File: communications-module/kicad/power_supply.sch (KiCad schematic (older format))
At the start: 25 parts, among them J1 IDC12, P2 USB_A, P3 USB_A, P4 USB_A, P5 BACKUP, U3 TPS2064, U4 PWR_CONN, U5 TPS2064

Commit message: Communications Module update
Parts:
- JP11, JP12, JP3, JP4: footprint (none) -> Socket_Strips:Socket_Strip_Straight_1x02_Pitch2.54mm
- P2, P3, P4: footprint (none) -> USB_A_receptacle:USB_A_receptacle
- R3: footprint (none) -> 0603_handsolder:0603_HandSoldering
- U4: footprint (none) -> Socket_Strips:Socket_Strip_Straight_2x05_Pitch2.54mm
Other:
- note added: "footprint ?"
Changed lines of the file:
@@
 F 0 "P3" H 6285 5150 50  0000 C CNN
 F 1 "USB_A" H 6025 5330 50  0000 C CNN
-F 2 "" V 6025 5030 60  0000 C CNN
+F 2 "USB_A_receptacle:USB_A_receptacle" V 6025 5030 60  0001 C CNN
 F 3 "" V 6025 5030 60  0000 C CNN
 	1    6075 5130
@@
 F 0 "P4" H 8270 5150 50  0000 C CNN
 F 1 "USB_A" H 8010 5330 50  0000 C CNN
-F 2 "" V 8010 5030 60  0000 C CNN
+F 2 "USB_A_receptacle:USB_A_receptacle" V 8010 5030 60  0001 C CNN
 F 3 "" V 8010 5030 60  0000 C CNN
 	1    8060 5130
@@
 F 0 "P2" H 4295 5150 50  0000 C CNN
 F 1 "USB_A" H 4035 5330 50  0000 C CNN
-F 2 "" V 4035 5030 60  0000 C CNN
+F 2 "USB_A_receptacle:USB_A_receptacle" V 4035 5030 60  0001 C CNN
 F 3 "" V 4035 5030 60  0000 C CNN
 	1    4085 5130
@@
 F 0 "JP3" H 4025 3570 50  0000 C CNN
 F 1 "Jumper_NC_Small" H 4035 3430 50  0001 C CNN
-F 2 "" H 4025 3490 60  0000 C CNN
+F 2 "Socket_Strips:Socket_Strip_Straight_1x02_Pitch2.54mm" H 4025 3490 60  0001 C CNN
 F 3 "" H 4025 3490 60  0000 C CNN
 	1    4025 3490
@@
 F 0 "JP11" H 7625 3310 50  0000 C CNN
 F 1 "Jumper_NC_Small" H 7635 3170 50  0001 C CNN
-F 2 "" H 7625 3230 60  0000 C CNN
+F 2 "Socket_Strips:Socket_Strip_Straight_1x02_Pitch2.54mm" H 7625 3230 60  0001 C CNN
 F 3 "" H 7625 3230 60  0000 C CNN
 	1    7625 3230
@@
 F 0 "JP12" H 7625 3495 50  0000 C CNN
 F 1 "Jumper_NC_Small" H 7635 3355 50  0001 C CNN
-F 2 "" H 7625 3415 60  0000 C CNN
+F 2 "Socket_Strips:Socket_Strip_Straight_1x02_Pitch2.54mm" H 7625 3415 60  0001 C CNN
 F 3 "" H 7625 3415 60  0000 C CNN
 	1    7625 3415
@@
 F 0 "U4" H 5035 2395 60  0000 C CNN
 F 1 "PWR_CONN" H 5360 1745 60  0000 C CNN
-F 2 "" H 5160 2470 60  0000 C CNN
+F 2 "Socket_Strips:Socket_Strip_Straight_2x05_Pitch2.54mm" H 5160 2470 60  0001 C CNN
 F 3 "" H 5160 2470 60  0000 C CNN
 	1    5360 2070
@@
 F 0 "R3" V 1815 2625 50  0000 C CNN
 F 1 "10K" V 1735 2625 50  0000 C CNN
-F 2 "" V 1665 2625 30  0000 C CNN
+F 2 "0603_handsolder:0603_HandSoldering" V 1665 2625 30  0001 C CNN
 F 3 "" H 1735 2625 30  0000 C CNN
 	1    1735 2625
@@
 F 0 "JP4" H 4025 3755 50  0000 C CNN
 F 1 "Jumper_NC_Small" H 4035 3615 50  0001 C CNN
-F 2 "" H 4025 3675 60  0000 C CNN
+F 2 "Socket_Strips:Socket_Strip_Straight_1x02_Pitch2.54mm" H 4025 3675 60  0001 C CNN
 F 3 "" H 4025 3675 60  0000 C CNN
 	1    4025 3675
@@
 Text HLabel 1945 1290 0    60   Input ~ 0
 ENABLE-5V
+Text Notes 5200 1695 0    118  ~ 0
+footprint ?
 $EndSCHEMATC

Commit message: Communications Module schematic update
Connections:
- net MCU_CTS renamed UART_CTS
- net MCU_RTS renamed UART_RTS
- net MCU_RX renamed UART_RX
- net MCU_TX renamed UART_TX
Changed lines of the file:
@@
 TWI_SDA
 $Comp
-L GND #PWR019
+L GND #PWR041
 U 1 1 589845A1
 P 4785 2270
-F 0 "#PWR019" H 4785 2020 50  0001 C CNN
+F 0 "#PWR041" H 4785 2020 50  0001 C CNN
 F 1 "GND" H 4785 2120 50  0000 C CNN
 F 2 "" H 4785 2270 60  0000 C CNN
@@
 $EndComp
 $Comp
-L GND #PWR020
+L GND #PWR042
 U 1 1 589845A7
 P 5935 2270
-F 0 "#PWR020" H 5935 2020 50  0001 C CNN
+F 0 "#PWR042" H 5935 2020 50  0001 C CNN
 F 1 "GND" H 5935 2120 50  0000 C CNN
 F 2 "" H 5935 2270 60  0000 C CNN
@@
 $EndComp
 $Comp
-L GND #PWR021
+L GND #PWR043
 U 1 1 589859EA
 P 6375 5030
-F 0 "#PWR021" H 6375 4780 50  0001 C CNN
+F 0 "#PWR043" H 6375 4780 50  0001 C CNN
 F 1 "GND" H 6375 4880 50  0000 C CNN
 F 2 "" H 6375 5030 60  0000 C CNN
@@
 $EndComp
 $Comp
-L GND #PWR022
+L GND #PWR044
 U 1 1 589859F7
 P 8315 5430
-F 0 "#PWR022" H 8315 5180 50  0001 C CNN
+F 0 "#PWR044" H 8315 5180 50  0001 C CNN
 F 1 "GND" H 8315 5280 50  0000 C CNN
 F 2 "" H 8315 5430 60  0000 C CNN
@@
 $EndComp
 $Comp
-L GND #PWR023
+L GND #PWR045
 U 1 1 58985A1D
 P 8360 5030
-F 0 "#PWR023" H 8360 4780 50  0001 C CNN
+F 0 "#PWR045" H 8360 4780 50  0001 C CNN
 F 1 "GND" H 8360 4880 50  0000 C CNN
 F 2 "" H 8360 5030 60  0000 C CNN
@@
 $EndComp
 $Comp
-L GND #PWR024
+L GND #PWR046
 U 1 1 58985A2A
 P 4340 5430
-F 0 "#PWR024" H 4340 5180 50  0001 C CNN
+F 0 "#PWR046" H 4340 5180 50  0001 C CNN
 F 1 "GND" H 4340 5280 50  0000 C CNN
 F 2 "" H 4340 5430 60  0000 C CNN
@@
 $EndComp
 $Comp
-L GND #PWR025
+L GND #PWR047
 U 1 1 58985A50
 P 4385 5030
-F 0 "#PWR025" H 4385 4780 50  0001 C CNN
+F 0 "#PWR047" H 4385 4780 50  0001 C CNN
 F 1 "GND" H 4385 4880 50  0000 C CNN
 F 2 "" H 4385 5030 60  0000 C CNN
@@
 $EndComp
 $Comp
-L GND #PWR026
+L GND #PWR048
 U 1 1 58985A5D
 P 6690 3760
-F 0 "#PWR026" H 6690 3510 50  0001 C CNN
+F 0 "#PWR048" H 6690 3510 50  0001 C CNN
 F 1 "GND" H 6690 3610 50  0000 C CNN
 F 2 "" H 6690 3760 60  0000 C CNN
@@
 	7615 4025 7740 4025
 $Comp
-L GND #PWR027
+L GND #PWR049
 U 1 1 58985A8F
 P 3065 3985
-F 0 "#PWR027" H 3065 3735 50  0001 C CNN
+F 0 "#PWR049" H 3065 3735 50  0001 C CNN
 F 1 "GND" H 3065 3835 50  0000 C CNN
 F 2 "" H 3065 3985 60  0000 C CNN
@@
 RESERV_5V
 $Comp
-L GND #PWR028
+L GND #PWR050
 U 1 1 58985AAE
 P 6330 5430
-F 0 "#PWR028" H 6330 5180 50  0001 C CNN
+F 0 "#PWR050" H 6330 5180 50  0001 C CNN
 F 1 "GND" H 6330 5280 50  0000 C CNN
 F 2 "" H 6330 5430 60  0000 C CNN
@@
 $EndComp
 $Comp
-L +5V #PWR029
+L +5V #PWR051
 U 1 1 58985ABE
 P 3925 3490
-F 0 "#PWR029" H 3925 3340 50  0001 C CNN
+F 0 "#PWR051" H 3925 3340 50  0001 C CNN
 F 1 "+5V" H 3925 3630 50  0000 C CNN
 F 2 "" H 3925 3490 60  0000 C CNN
@@
 $EndComp
 $Comp
-L +5V #PWR030
+L +5V #PWR052
 U 1 1 58985AD9
 P 7525 3230
-F 0 "#PWR030" H 7525 3080 50  0001 C CNN
+F 0 "#PWR052" H 7525 3080 50  0001 C CNN
 F 1 "+5V" H 7525 3370 50  0000 C CNN
 F 2 "" H 7525 3230 60  0000 C CNN
@@
 $EndComp
 $Comp
-L +5V #PWR031
+L +5V #PWR053
 U 1 1 58985AE6
 P 7525 3415
-F 0 "#PWR031" H 7525 3265 50  0001 C CNN
+F 0 "#PWR053" H 7525 3265 50  0001 C CNN
 F 1 "+5V" H 7525 3555 50  0000 C CNN
 F 2 "" H 7525 3415 60  0000 C CNN
@@
 5V
 $Comp
-L +5V #PWR032
+L +5V #PWR054
 U 1 1 58988CC2
 P 8200 1550
-F 0 "#PWR032" H 8200 1400 50  0001 C CNN
+F 0 "#PWR054" H 8200 1400 50  0001 C CNN
 F 1 "+5V" H 8200 1690 50  0000 C CNN
 F 2 "" H 8200 1550 60  0000 C CNN
@@
 $EndComp
 $Comp
-L +3.3V #PWR033
+L +3.3V #PWR055
 U 1 1 58989B65
 P 8215 1775
-F 0 "#PWR033" H 8215 1625 50  0001 C CNN
+F 0 "#PWR055" H 8215 1625 50  0001 C CNN
 F 1 "+3.3V" H 8215 1915 50  0000 C CNN
 F 2 "" H 8215 1775 60  0000 C CNN
@@
 TWI_SCL
 $Comp
-L +5V #PWR034
+L +5V #PWR056
 U 1 1 589845B4
 P 4265 1815
-F 0 "#PWR034" H 4265 1665 50  0001 C CNN
+F 0 "#PWR056" H 4265 1665 50  0001 C CNN
 F 1 "+5V" H 4265 1955 50  0000 C CNN
 F 2 "" H 4265 1815 60  0000 C CNN
@@
 $EndComp
 $Comp
-L +3.3V #PWR035
+L +3.3V #PWR057
 U 1 1 589845AE
 P 4110 1975
-F 0 "#PWR035" H 4110 1825 50  0001 C CNN
+F 0 "#PWR057" H 4110 1825 50  0001 C CNN
 F 1 "+3.3V" H 4110 2115 50  0000 C CNN
 F 2 "" H 4110 1975 60  0000 C CNN
@@
 BACKUP_5V
 $Comp
-L GND #PWR036
+L GND #PWR058
 U 1 1 589977EF
 P 9700 4535
-F 0 "#PWR036" H 9700 4285 50  0001 C CNN
+F 0 "#PWR058" H 9700 4285 50  0001 C CNN
 F 1 "GND" H 9700 4385 50  0000 C CNN
 F 2 "" H 9700 4535 60  0000 C CNN
@@
 AIR_5V
 $Comp
-L GND #PWR037
+L GND #PWR059
 U 1 1 58A00F9B
 P 8195 1320
-F 0 "#PWR037" H 8195 1070 50  0001 C CNN
+F 0 "#PWR059" H 8195 1070 50  0001 C CNN
 F 1 "GND" H 8195 1170 50  0000 C CNN
 F 2 "" H 8195 1320 60  0000 C CNN
@@
 $EndComp
 $Comp
-L +3.3V #PWR038
+L +3.3V #PWR060
 U 1 1 58999FE9
 P 1585 2625
-F 0 "#PWR038" H 1585 2475 50  0001 C CNN
+F 0 "#PWR060" H 1585 2475 50  0001 C CNN
 F 1 "+3.3V" H 1585 2765 50  0000 C CNN
 F 2 "" H 1585 2625 60  0000 C CNN
@@
 SPI_SCLK
 $Comp
-L GND #PWR039
+L GND #PWR061
 U 1 1 58A15D45
 P 2385 5215
-F 0 "#PWR039" H 2385 4965 50  0001 C CNN
+F 0 "#PWR061" H 2385 4965 50  0001 C CNN
 F 1 "GND" H 2385 5065 50  0000 C CNN
 F 2 "" H 2385 5215 60  0000 C CNN
@@
 	1905 5775 1710 5775
 Text GLabel 1710 5675 0    60   Input ~ 0
-MCU_TX
+UART_TX
 Text GLabel 2310 5675 2    60   Input ~ 0
-MCU_RX
+UART_RX
 Text GLabel 1710 5775 0    60   Input ~ 0
-MCU_CTS
+UART_CTS
 Text GLabel 2310 5775 2    60   Input ~ 0
-MCU_RTS
+UART_RTS
 Wire Wire Line
 	2155 5375 2310 5375
@@
 SPI_SCLK
 Text GLabel 9730 3355 2    60   Input ~ 0
-MCU_TX
+UART_TX
 Text GLabel 9730 3455 2    60   Input ~ 0
-MCU_CTS
+UART_CTS
 Text GLabel 9730 2840 2    60   Input ~ 0
 SPI_MOSI
@@
 SPI_CS
 Text GLabel 9730 2940 2    60   Input ~ 0
-MCU_RX
+UART_RX
 Text GLabel 9730 3040 2    60   Input ~ 0
-MCU_RTS
+UART_RTS
 Text HLabel 9730 2740 0    60   Input ~ 0
 SPI_CS
@@
 SPI_MOSI
 Text HLabel 9730 2940 0    60   Input ~ 0
-MCU_RX
+UART_RX
 Text HLabel 9730 3040 0    60   Input ~ 0
-MCU_RTS
+UART_RTS
 Text HLabel 9730 3155 0    60   Input ~ 0
 SPI_SCLK
@@
 SPI_MISO
 Text HLabel 9730 3355 0    60   Input ~ 0
-MCU_TX
+UART_TX
 Text HLabel 9730 3455 0    60   Input ~ 0
-MCU_CTS
+UART_CTS
 Text GLabel 1955 1670 2    60   Input ~ 0
 ENABLE-AIR
 $Comp
-L +5V #PWR040
+L +5V #PWR062
 U 1 1 58985A95
 P 2880 3985
-F 0 "#PWR040" H 2880 3835 50  0001 C CNN
+F 0 "#PWR062" H 2880 3835 50  0001 C CNN
 F 1 "+5V" H 2880 4125 50  0000 C CNN
 F 2 "" H 2880 3985 60  0000 C CNN
@@
 $EndComp
 $Comp
-L +5V #PWR041
+L +5V #PWR063
 U 1 1 58985ACB
 P 3925 3675
-F 0 "#PWR041" H 3925 3525 50  0001 C CNN
+F 0 "#PWR063" H 3925 3525 50  0001 C CNN
 F 1 "+5V" H 3925 3815 50  0000 C CNN
 F 2 "" H 3925 3675 60  0000 C CNN
@@
 BACKUP_5V
 $Comp
-L +5V #PWR042
+L +5V #PWR064
 U 1 1 58985A63
 P 6505 3760
-F 0 "#PWR042" H 6505 3610 50  0001 C CNN
+F 0 "#PWR064" H 6505 3610 50  0001 C CNN
 F 1 "+5V" H 6505 3900 50  0000 C CNN
 F 2 "" H 6505 3760 60  0000 C CNN
@@
 Text Notes 5200 1695 0    118  ~ 0
 footprint ?
+Text GLabel 1335 7385 0    60   Input ~ 0
+GEIGER_5V
+Text GLabel 2200 7390 0    60   Input ~ 0
+AIR_5V
+Text GLabel 3220 7405 0    60   Input ~ 0
+RESERV_5V
+$Comp
+L PWR_FLAG #FLG065
+U 1 1 589AC172
+P 1335 7385
+F 0 "#FLG065" H 1335 7480 50  0001 C CNN
+F 1 "PWR_FLAG" H 1335 7565 50  0000 C CNN
+F 2 "" H 1335 7385 60  0000 C CNN
+F 3 "" H 1335 7385 60  0000 C CNN
+	1    1335 7385
+	0    1    1    0
+$EndComp
+$Comp
+L PWR_FLAG #FLG066
+U 1 1 589AC39B
+P 2200 7390
+F 0 "#FLG066" H 2200 7485 50  0001 C CNN
+F 1 "PWR_FLAG" H 2200 7570 50  0000 C CNN
+F 2 "" H 2200 7390 60  0000 C CNN
+F 3 "" H 2200 7390 60  0000 C CNN
+	1    2200 7390
+	0    1    1    0
+$EndComp
+$Comp
+L PWR_FLAG #FLG067
+U 1 1 589AC824
+P 3220 7405
+F 0 "#FLG067" H 3220 7500 50  0001 C CNN
+F 1 "PWR_FLAG" H 3220 7585 50  0000 C CNN
+F 2 "" H 3220 7405 60  0000 C CNN
+F 3 "" H 3220 7405 60  0000 C CNN
+	1    3220 7405
+	0    1    1    0
+$EndComp
 $EndSCHEMATC

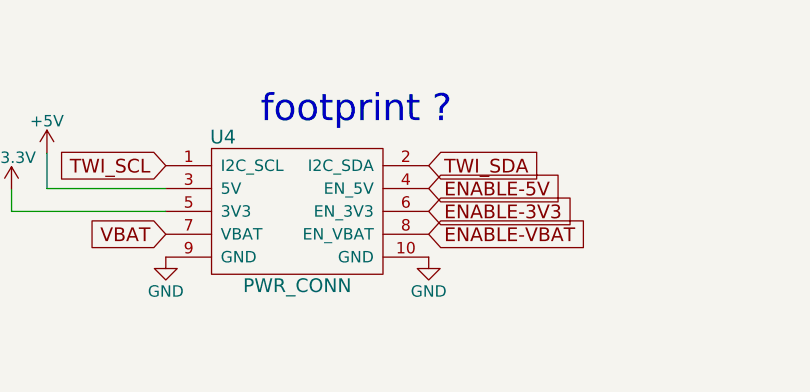
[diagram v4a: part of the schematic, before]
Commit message: Communications Module footprints update
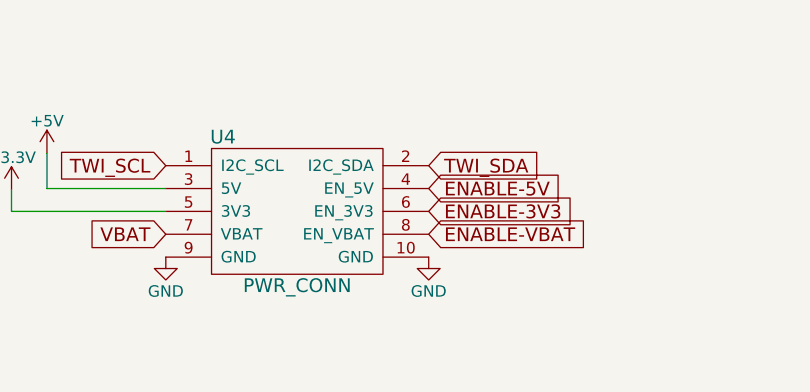
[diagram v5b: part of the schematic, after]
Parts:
- JP1, JP10, JP13, JP14, JP15, JP16, JP2, JP5, JP6, JP7, JP8, JP9: footprint (none) -> Socket_Strips:Socket_Strip_Straight_1x02_Pitch2.54mm
- U4: footprint Socket_Strips:Socket_Strip_Straight_2x05_Pitch2.54mm -> IDC10_connector:IDC10_connector
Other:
- note removed: "footprint ?"
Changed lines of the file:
@@
 F 0 "JP7" H 5820 5680 50  0000 C CNN
 F 1 "Jumper_NC_Small" H 5830 5540 50  0001 C CNN
-F 2 "" H 5820 5600 60  0000 C CNN
+F 2 "Socket_Strips:Socket_Strip_Straight_1x02_Pitch2.54mm" H 5820 5600 60  0001 C CNN
 F 3 "" H 5820 5600 60  0000 C CNN
 	1    5820 5600
@@
 F 0 "JP8" H 5820 5645 50  0000 C CNN
 F 1 "Jumper_NC_Small" H 5830 5655 50  0001 C CNN
-F 2 "" H 5820 5715 60  0000 C CNN
+F 2 "Socket_Strips:Socket_Strip_Straight_1x02_Pitch2.54mm" H 5820 5715 60  0001 C CNN
 F 3 "" H 5820 5715 60  0000 C CNN
 	1    5820 5715
@@
 F 0 "JP9" H 6220 5680 50  0000 C CNN
 F 1 "Jumper_NC_Small" H 6230 5540 50  0001 C CNN
-F 2 "" H 6220 5600 60  0000 C CNN
+F 2 "Socket_Strips:Socket_Strip_Straight_1x02_Pitch2.54mm" H 6220 5600 60  0001 C CNN
 F 3 "" H 6220 5600 60  0000 C CNN
 	1    6220 5600
@@
 F 0 "JP10" H 6220 5645 50  0000 C CNN
 F 1 "Jumper_NC_Small" H 6230 5655 50  0001 C CNN
-F 2 "" H 6220 5715 60  0000 C CNN
+F 2 "Socket_Strips:Socket_Strip_Straight_1x02_Pitch2.54mm" H 6220 5715 60  0001 C CNN
 F 3 "" H 6220 5715 60  0000 C CNN
 	1    6220 5715
@@
 F 0 "JP13" H 7805 5680 50  0000 C CNN
 F 1 "Jumper_NC_Small" H 7815 5540 50  0001 C CNN
-F 2 "" H 7805 5600 60  0000 C CNN
+F 2 "Socket_Strips:Socket_Strip_Straight_1x02_Pitch2.54mm" H 7805 5600 60  0001 C CNN
 F 3 "" H 7805 5600 60  0000 C CNN
 	1    7805 5600
@@
 F 0 "JP14" H 7805 5645 50  0000 C CNN
 F 1 "Jumper_NC_Small" H 7815 5655 50  0001 C CNN
-F 2 "" H 7805 5715 60  0000 C CNN
+F 2 "Socket_Strips:Socket_Strip_Straight_1x02_Pitch2.54mm" H 7805 5715 60  0001 C CNN
 F 3 "" H 7805 5715 60  0000 C CNN
 	1    7805 5715
@@
 F 0 "JP15" H 8205 5680 50  0000 C CNN
 F 1 "Jumper_NC_Small" H 8215 5540 50  0001 C CNN
-F 2 "" H 8205 5600 60  0000 C CNN
+F 2 "Socket_Strips:Socket_Strip_Straight_1x02_Pitch2.54mm" H 8205 5600 60  0001 C CNN
 F 3 "" H 8205 5600 60  0000 C CNN
 	1    8205 5600
@@
 F 0 "JP16" H 8205 5645 50  0000 C CNN
 F 1 "Jumper_NC_Small" H 8215 5655 50  0001 C CNN
-F 2 "" H 8205 5715 60  0000 C CNN
+F 2 "Socket_Strips:Socket_Strip_Straight_1x02_Pitch2.54mm" H 8205 5715 60  0001 C CNN
 F 3 "" H 8205 5715 60  0000 C CNN
 	1    8205 5715
@@
 F 0 "JP1" H 3830 5680 50  0000 C CNN
 F 1 "Jumper_NC_Small" H 3840 5540 50  0001 C CNN
-F 2 "" H 3830 5600 60  0000 C CNN
+F 2 "Socket_Strips:Socket_Strip_Straight_1x02_Pitch2.54mm" H 3830 5600 60  0001 C CNN
 F 3 "" H 3830 5600 60  0000 C CNN
 	1    3830 5600
@@
 F 0 "JP2" H 3830 5645 50  0000 C CNN
 F 1 "Jumper_NC_Small" H 3840 5655 50  0001 C CNN
-F 2 "" H 3830 5715 60  0000 C CNN
+F 2 "Socket_Strips:Socket_Strip_Straight_1x02_Pitch2.54mm" H 3830 5715 60  0001 C CNN
 F 3 "" H 3830 5715 60  0000 C CNN
 	1    3830 5715
@@
 F 0 "JP5" H 4230 5680 50  0000 C CNN
 F 1 "Jumper_NC_Small" H 4240 5540 50  0001 C CNN
-F 2 "" H 4230 5600 60  0000 C CNN
+F 2 "Socket_Strips:Socket_Strip_Straight_1x02_Pitch2.54mm" H 4230 5600 60  0001 C CNN
 F 3 "" H 4230 5600 60  0000 C CNN
 	1    4230 5600
@@
 F 0 "JP6" H 4230 5645 50  0000 C CNN
 F 1 "Jumper_NC_Small" H 4240 5655 50  0001 C CNN
-F 2 "" H 4230 5715 60  0000 C CNN
+F 2 "Socket_Strips:Socket_Strip_Straight_1x02_Pitch2.54mm" H 4230 5715 60  0001 C CNN
 F 3 "" H 4230 5715 60  0000 C CNN
 	1    4230 5715
@@
 F 0 "U4" H 5035 2395 60  0000 C CNN
 F 1 "PWR_CONN" H 5360 1745 60  0000 C CNN
-F 2 "Socket_Strips:Socket_Strip_Straight_2x05_Pitch2.54mm" H 5160 2470 60  0001 C CNN
+F 2 "IDC10_connector:IDC10_connector" H 5160 2470 60  0001 C CNN
 F 3 "" H 5160 2470 60  0000 C CNN
 	1    5360 2070
@@
 Text HLabel 1945 1290 0    60   Input ~ 0
 ENABLE-5V
-Text Notes 5200 1695 0    118  ~ 0
-footprint ?
 Text GLabel 1335 7385 0    60   Input ~ 0
 GEIGER_5V
